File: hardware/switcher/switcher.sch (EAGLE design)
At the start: 3 parts, among them IC1 L293E

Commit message: update schematics
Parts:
- removed G1: AB9V, battery:AB9V
- added BAT1: (no value), SparkFun-Connectors:BC9VPC
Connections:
- net P1.3 renamed P2.4
- net 9V: now also BAT1.V+; no longer G1.+
- net GND: now also BAT1.V-; no longer G1.-
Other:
- note added: "5V Regulator"
- note added: "9V Battery Holder"
- note added: "Board for holding motor driver and power source and connects both to the motor and to the Green Board"
- note added: "Derailleurs Switcher Board Alice Stevens and Mackenzie Binns"
- note added: "H-Bridge Motor Controller"
- note added: "LM7805"
- note added: "This board connects to the Green Board via mated headers."
- note removed: "Custom board for motor module - Alice Stevens"

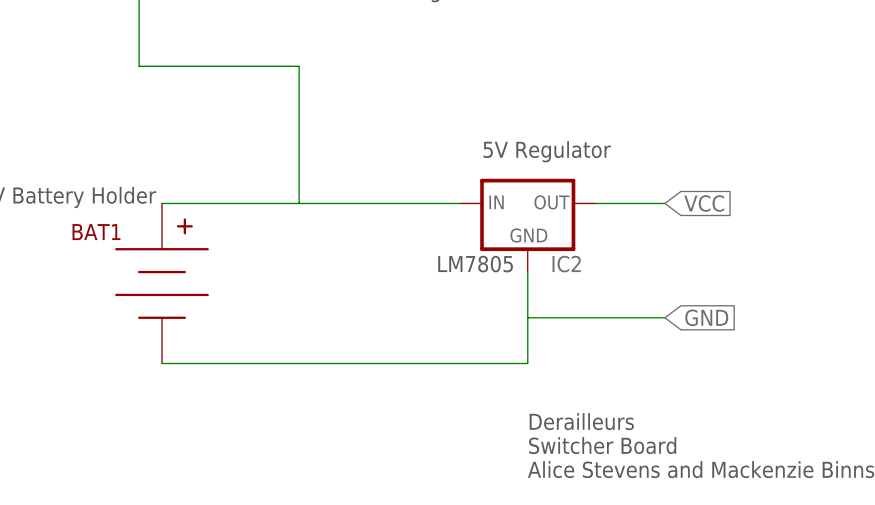
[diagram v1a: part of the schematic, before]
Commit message: add capacitors
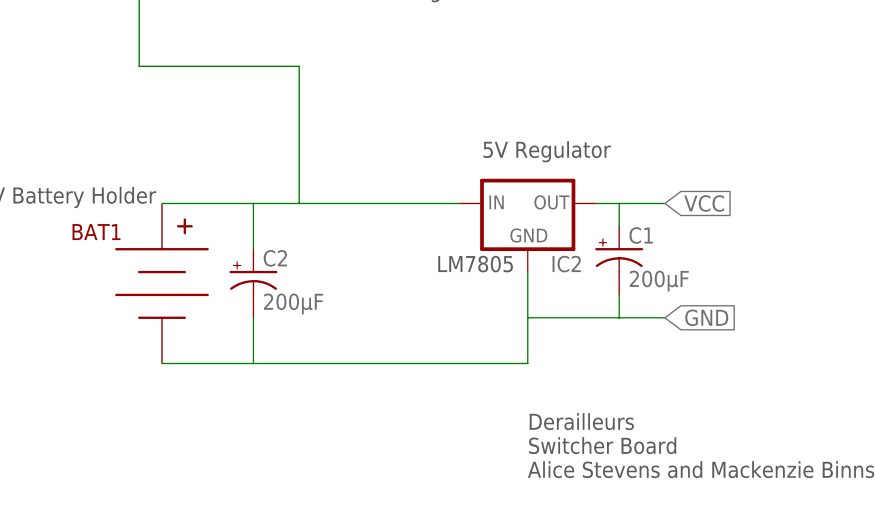
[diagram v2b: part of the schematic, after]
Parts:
- added C1, C2: 200µF, SparkFun-Capacitors:CAP_POLPTH1
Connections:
- net 9V: now also C2.+
- net GND: now also C1.-, C2.-
- net VCC: now also C1.+
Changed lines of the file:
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@@
 <part name="IC2" library="v-reg" deviceset="78XXL" device=""/>
 <part name="BAT1" library="SparkFun-Connectors" deviceset="BC9VPC" device=""/>
+<part name="C1" library="SparkFun-Capacitors" deviceset="CAP_POL" device="PTH1" value="200µF"/>
+<part name="C2" library="SparkFun-Capacitors" deviceset="CAP_POL" device="PTH1" value="200µF"/>
 </parts>
 <sheets>
@@
 <instance part="IC2" gate="A" x="76.2" y="10.16"/>
 <instance part="BAT1" gate="G$1" x="35.56" y="2.54"/>
+<instance part="C1" gate="G$1" x="86.36" y="5.08"/>
+<instance part="C2" gate="G$1" x="45.72" y="2.54"/>
 </instances>
 <busses>
@@
 <segment>
 <pinref part="IC2" gate="A" pin="OUT"/>
-<wire x1="83.82" y1="10.16" x2="91.44" y2="10.16" width="0.1524" layer="91"/>
+<wire x1="83.82" y1="10.16" x2="86.36" y2="10.16" width="0.1524" layer="91"/>
 <label x="91.44" y="10.16" size="1.778" layer="95" xref="yes"/>
+<pinref part="C1" gate="G$1" pin="+"/>
+<wire x1="86.36" y1="10.16" x2="91.44" y2="10.16" width="0.1524" layer="91"/>
+<wire x1="86.36" y1="7.62" x2="86.36" y2="10.16" width="0.1524" layer="91"/>
 </segment>
 </net>
@@
 <pinref part="IC2" gate="A" pin="GND"/>
 <wire x1="76.2" y1="-2.54" x2="76.2" y2="2.54" width="0.1524" layer="91"/>
-<wire x1="76.2" y1="-2.54" x2="91.44" y2="-2.54" width="0.1524" layer="91"/>
+<wire x1="76.2" y1="-2.54" x2="86.36" y2="-2.54" width="0.1524" layer="91"/>
 <label x="91.44" y="-2.54" size="1.778" layer="95" xref="yes"/>
 <pinref part="BAT1" gate="G$1" pin="V-"/>
-<wire x1="35.56" y1="-7.62" x2="76.2" y2="-7.62" width="0.1524" layer="91"/>
+<wire x1="86.36" y1="-2.54" x2="91.44" y2="-2.54" width="0.1524" layer="91"/>
+<wire x1="35.56" y1="-7.62" x2="45.72" y2="-7.62" width="0.1524" layer="91"/>
+<wire x1="45.72" y1="-7.62" x2="76.2" y2="-7.62" width="0.1524" layer="91"/>
 <wire x1="76.2" y1="-7.62" x2="76.2" y2="-2.54" width="0.1524" layer="91"/>
+<pinref part="C2" gate="G$1" pin="-"/>
+<wire x1="45.72" y1="-2.54" x2="45.72" y2="-7.62" width="0.1524" layer="91"/>
+<pinref part="C1" gate="G$1" pin="-"/>
+<wire x1="86.36" y1="0" x2="86.36" y2="-2.54" width="0.1524" layer="91"/>
 </segment>
 </net>
@@
 <wire x1="33.02" y1="25.4" x2="50.8" y2="25.4" width="0.1524" layer="91"/>
 <pinref part="IC2" gate="A" pin="IN"/>
-<wire x1="35.56" y1="10.16" x2="50.8" y2="10.16" width="0.1524" layer="91"/>
+<wire x1="35.56" y1="10.16" x2="45.72" y2="10.16" width="0.1524" layer="91"/>
+<wire x1="45.72" y1="10.16" x2="50.8" y2="10.16" width="0.1524" layer="91"/>
 <wire x1="50.8" y1="10.16" x2="68.58" y2="10.16" width="0.1524" layer="91"/>
 <wire x1="50.8" y1="25.4" x2="50.8" y2="10.16" width="0.1524" layer="91"/>
 <pinref part="BAT1" gate="G$1" pin="V+"/>
+<pinref part="C2" gate="G$1" pin="+"/>
+<wire x1="45.72" y1="5.08" x2="45.72" y2="10.16" width="0.1524" layer="91"/>
 </segment>
 </net>

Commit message: finish boards
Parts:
- removed BAT1: (no value), SparkFun-Connectors:BC9VPC
- added BLUE, RED, WHITE, YELLOW: (no value), SparkFun-Connectors:M01PTH
- added GND, VCC: (no value), SparkFun-Connectors:M03PTH
- added J1, J2: (no value), SparkFun-Connectors:M20
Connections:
- removed net P2.4: IC1.4A
- new net P2.5: IC1.4A, J1.3
- net 9V: no longer BAT1.V+
- net GND: now also GND.1, GND.2, GND.3; no longer BAT1.V-
- net MOTOR-BLUE: now also BLUE.1
- net MOTOR-RED: now also RED.1
- net MOTOR-WHITE: now also WHITE.1
- net MOTOR-YELLOW: now also YELLOW.1
- net P3.4: now also J1.10
- net P3.5: now also J1.11
- net P3.6: now also J1.12
- net VCC: now also VCC.1, VCC.2, VCC.3
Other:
- note removed: "9V Battery Holder"
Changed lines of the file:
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@@
 <part name="IC1" library="texas" deviceset="L293E" device=""/>
 <part name="IC2" library="v-reg" deviceset="78XXL" device=""/>
-<part name="BAT1" library="SparkFun-Connectors" deviceset="BC9VPC" device=""/>
 <part name="C1" library="SparkFun-Capacitors" deviceset="CAP_POL" device="PTH1" value="200µF"/>
 <part name="C2" library="SparkFun-Capacitors" deviceset="CAP_POL" device="PTH1" value="200µF"/>
+<part name="J1" library="SparkFun-Connectors" deviceset="M20" device=""/>
+<part name="J2" library="SparkFun-Connectors" deviceset="M20" device=""/>
+<part name="GND" library="SparkFun-Connectors" deviceset="M03" device="PTH"/>
+<part name="VCC" library="SparkFun-Connectors" deviceset="M03" device="PTH"/>
+<part name="RED" library="SparkFun-Connectors" deviceset="M01" device="PTH"/>
+<part name="YELLOW" library="SparkFun-Connectors" deviceset="M01" device="PTH"/>
+<part name="BLUE" library="SparkFun-Connectors" deviceset="M01" device="PTH"/>
+<part name="WHITE" library="SparkFun-Connectors" deviceset="M01" device="PTH"/>
 </parts>
 <sheets>
 <sheet>
 <plain>
-<frame x1="-7.62" y1="-25.4" x2="119.38" y2="96.52" columns="8" rows="5" layer="91"/>
 <text x="-2.54" y="88.9" size="1.778" layer="97">Board for holding motor driver and power source and connects both to the motor and to the Green Board</text>
 <text x="58.42" y="33.02" size="1.778" layer="97">H-Bridge Motor Controller</text>
 <text x="66.04" y="2.54" size="1.778" layer="97">LM7805</text>
 <text x="71.12" y="15.24" size="1.778" layer="97">5V Regulator</text>
-<text x="15.24" y="10.16" size="1.778" layer="97">9V Battery Holder</text>
 <text x="-2.54" y="83.82" size="1.778" layer="97">This board connects to the Green Board via mated headers.</text>
-<text x="76.2" y="-20.32" size="1.778" layer="97">Derailleurs
+<text x="129.54" y="-20.32" size="1.778" layer="97">Derailleurs
 Switcher Board
 Alice Stevens and Mackenzie Binns</text>
+<frame x1="-20.32" y1="-27.94" x2="180.34" y2="96.52" columns="8" rows="5" layer="91"/>
 </plain>
 <instances>
 <instance part="IC1" gate="G$1" x="55.88" y="55.88"/>
 <instance part="IC2" gate="A" x="76.2" y="10.16"/>
-<instance part="BAT1" gate="G$1" x="35.56" y="2.54"/>
 <instance part="C1" gate="G$1" x="86.36" y="5.08"/>
 <instance part="C2" gate="G$1" x="45.72" y="2.54"/>
+<instance part="J1" gate="G$1" x="114.3" y="22.86"/>
+<instance part="J2" gate="G$1" x="147.32" y="22.86"/>
+<instance part="GND" gate="J$1" x="116.84" y="7.62"/>
+<instance part="VCC" gate="J$1" x="149.86" y="7.62"/>
+<instance part="RED" gate="G$1" x="-10.16" y="7.62"/>
+<instance part="YELLOW" gate="G$1" x="-10.16" y="0"/>
+<instance part="BLUE" gate="G$1" x="-10.16" y="15.24"/>
+<instance part="WHITE" gate="G$1" x="-10.16" y="22.86"/>
 </instances>
 <busses>
@@
 <wire x1="86.36" y1="7.62" x2="86.36" y2="10.16" width="0.1524" layer="91"/>
 </segment>
+<segment>
+<pinref part="VCC" gate="J$1" pin="1"/>
+<wire x1="157.48" y1="5.08" x2="160.02" y2="5.08" width="0.1524" layer="91"/>
+<wire x1="160.02" y1="5.08" x2="160.02" y2="7.62" width="0.1524" layer="91"/>
+<pinref part="VCC" gate="J$1" pin="2"/>
+<wire x1="157.48" y1="7.62" x2="160.02" y2="7.62" width="0.1524" layer="91"/>
+<pinref part="VCC" gate="J$1" pin="3"/>
+<wire x1="157.48" y1="10.16" x2="160.02" y2="10.16" width="0.1524" layer="91"/>
+<wire x1="160.02" y1="10.16" x2="160.02" y2="7.62" width="0.1524" layer="91"/>
+<label x="160.02" y="7.62" size="1.778" layer="95" xref="yes"/>
+</segment>
 </net>
 <net name="P3.4" class="0">
@@
 <label x="33.02" y="68.58" size="1.778" layer="95" rot="MR0" xref="yes"/>
 </segment>
+<segment>
+<pinref part="J1" gate="G$1" pin="10"/>
+<wire x1="124.46" y1="50.8" x2="127" y2="50.8" width="0.1524" layer="91"/>
+<label x="127" y="50.8" size="1.778" layer="95" xref="yes"/>
+</segment>
 </net>
 <net name="MOTOR-RED" class="0">
@@
 <wire x1="40.64" y1="63.5" x2="33.02" y2="63.5" width="0.1524" layer="91"/>
 <label x="33.02" y="63.5" size="1.778" layer="95" rot="MR0" xref="yes"/>
+</segment>
+<segment>
+<pinref part="RED" gate="G$1" pin="1"/>
+<wire x1="-2.54" y1="7.62" x2="2.54" y2="7.62" width="0.1524" layer="91"/>
+<label x="2.54" y="7.62" size="1.778" layer="95" xref="yes"/>
 </segment>
 </net>
@@
 <wire x1="76.2" y1="-2.54" x2="86.36" y2="-2.54" width="0.1524" layer="91"/>
 <label x="91.44" y="-2.54" size="1.778" layer="95" xref="yes"/>
-<pinref part="BAT1" gate="G$1" pin="V-"/>
 <wire x1="86.36" y1="-2.54" x2="91.44" y2="-2.54" width="0.1524" layer="91"/>
 <wire x1="35.56" y1="-7.62" x2="45.72" y2="-7.62" width="0.1524" layer="91"/>
@@
 <pinref part="C1" gate="G$1" pin="-"/>
 <wire x1="86.36" y1="0" x2="86.36" y2="-2.54" width="0.1524" layer="91"/>
+<label x="35.56" y="-7.62" size="1.778" layer="95" rot="R180" xref="yes"/>
+</segment>
+<segment>
+<pinref part="GND" gate="J$1" pin="1"/>
+<wire x1="124.46" y1="5.08" x2="127" y2="5.08" width="0.1524" layer="91"/>
+<wire x1="127" y1="5.08" x2="127" y2="7.62" width="0.1524" layer="91"/>
+<pinref part="GND" gate="J$1" pin="2"/>
+<wire x1="127" y1="7.62" x2="124.46" y2="7.62" width="0.1524" layer="91"/>
+<pinref part="GND" gate="J$1" pin="3"/>
+<wire x1="124.46" y1="10.16" x2="127" y2="10.16" width="0.1524" layer="91"/>
+<wire x1="127" y1="10.16" x2="127" y2="7.62" width="0.1524" layer="91"/>
+<label x="127" y="7.62" size="1.778" layer="95" xref="yes"/>
 </segment>
 </net>
@@
 <label x="33.02" y="48.26" size="1.778" layer="95" rot="MR0" xref="yes"/>
 </segment>
+<segment>
+<pinref part="BLUE" gate="G$1" pin="1"/>
+<wire x1="-2.54" y1="15.24" x2="2.54" y2="15.24" width="0.1524" layer="91"/>
+<label x="2.54" y="15.24" size="1.778" layer="95" xref="yes"/>
+</segment>
 </net>
 <net name="P3.5" class="0">
@@
 <wire x1="40.64" y1="43.18" x2="33.02" y2="43.18" width="0.1524" layer="91"/>
 <label x="33.02" y="43.18" size="1.778" layer="95" rot="MR0" xref="yes"/>
+</segment>
+<segment>
+<pinref part="J1" gate="G$1" pin="11"/>
+<wire x1="124.46" y1="53.34" x2="134.62" y2="53.34" width="0.1524" layer="91"/>
+<label x="134.62" y="53.34" size="1.778" layer="95" xref="yes"/>
 </segment>
 </net>
@@
 <wire x1="50.8" y1="10.16" x2="68.58" y2="10.16" width="0.1524" layer="91"/>
 <wire x1="50.8" y1="25.4" x2="50.8" y2="10.16" width="0.1524" layer="91"/>
-<pinref part="BAT1" gate="G$1" pin="V+"/>
 <pinref part="C2" gate="G$1" pin="+"/>
 <wire x1="45.72" y1="5.08" x2="45.72" y2="10.16" width="0.1524" layer="91"/>
-</segment>
-</net>
-<net name="P2.4" class="0">
+<label x="35.56" y="10.16" size="1.778" layer="95" rot="R180" xref="yes"/>
+</segment>
+</net>
+<net name="P2.5" class="0">
 <segment>
 <pinref part="IC1" gate="G$1" pin="4A"/>
@@
 <label x="78.74" y="68.58" size="1.778" layer="95" xref="yes"/>
 </segment>
+<segment>
+<pinref part="J1" gate="G$1" pin="3"/>
+<wire x1="124.46" y1="33.02" x2="127" y2="33.02" width="0.1524" layer="91"/>
+<label x="127" y="33.02" size="1.778" layer="95" xref="yes"/>
+</segment>
 </net>
 <net name="MOTOR-YELLOW" class="0">
@@
 <label x="78.74" y="63.5" size="1.778" layer="95" xref="yes"/>
 </segment>
+<segment>
+<pinref part="YELLOW" gate="G$1" pin="1"/>
+<wire x1="-2.54" y1="0" x2="2.54" y2="0" width="0.1524" layer="91"/>
+<label x="2.54" y="0" size="1.778" layer="95" xref="yes"/>
+</segment>
 </net>
 <net name="MOTOR-WHITE" class="0">
@@
 <label x="78.74" y="48.26" size="1.778" layer="95" xref="yes"/>
 </segment>
+<segment>
+<pinref part="WHITE" gate="G$1" pin="1"/>
+<wire x1="-2.54" y1="22.86" x2="2.54" y2="22.86" width="0.1524" layer="91"/>
+<label x="2.54" y="22.86" size="1.778" layer="95" xref="yes"/>
+</segment>
 </net>
 <net name="P3.6" class="0">
@@
 <label x="78.74" y="43.18" size="1.778" layer="95" xref="yes"/>
 </segment>
-</net>
+<segment>
+<pinref part="J1" gate="G$1" pin="12"/>
+<wire x1="124.46" y1="55.88" x2="127" y2="55.88" width="0.1524" layer="91"/>
+<label x="127" y="55.88" size="1.778" layer="95" xref="yes"/>
+</segment>
+</net>

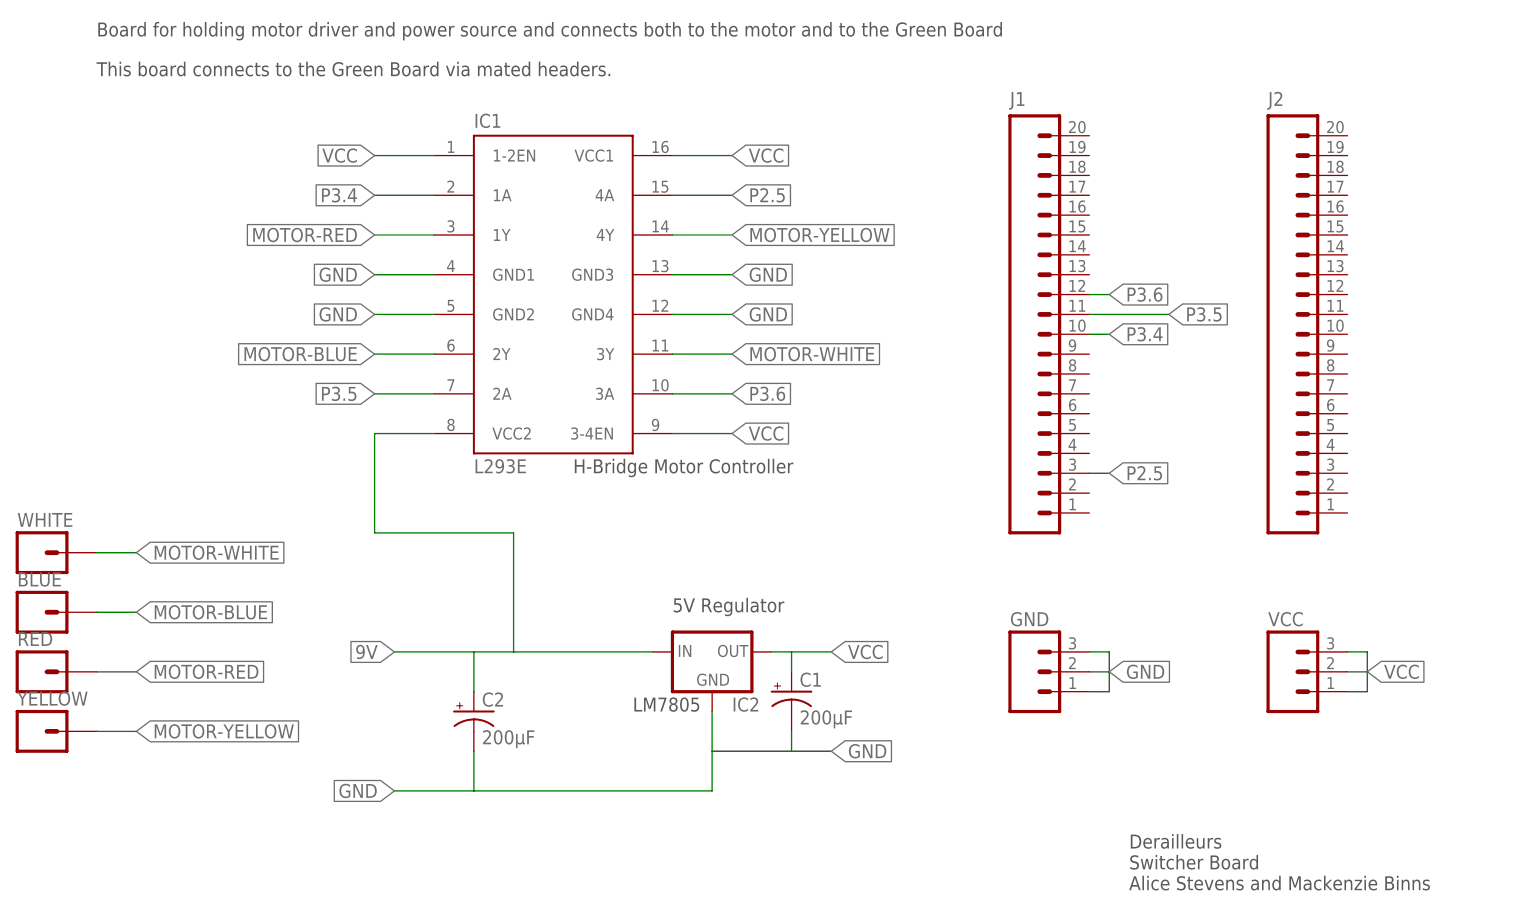
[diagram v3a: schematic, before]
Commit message: Finish routing all boards, schematics are consitant, and all deliverable requirements are met..
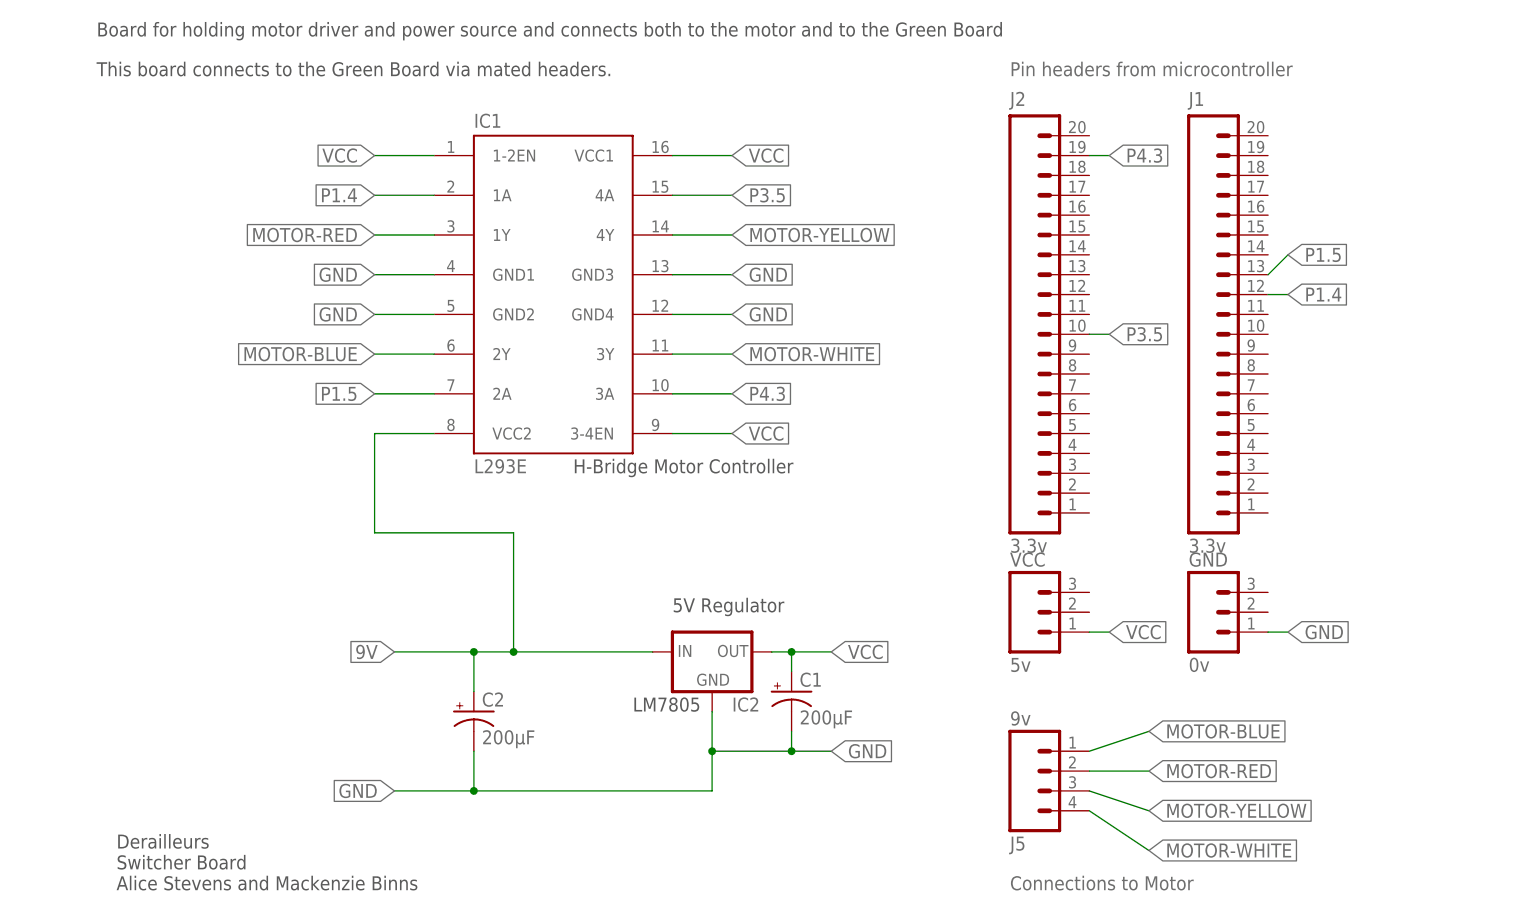
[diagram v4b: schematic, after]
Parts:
- removed BLUE, RED, WHITE, YELLOW: (no value), SparkFun-Connectors:M01PTH
- added J5: 9v, SparkFun-Connectors:M04PTH
- GND: value (none) -> 0v
- J1, J2: value (none) -> 3.3v
- VCC: value (none) -> 5v
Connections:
- removed net P2.5: IC1.4A, J1.3
- removed net P3.4: IC1.1A, J1.10
- removed net P3.6: IC1.3A, J1.12
- new net P1.4: IC1.1A, J1.12
- new net P1.5: IC1.2A, J1.13
- new net P4.3: IC1.3A, J2.19
- net GND: no longer GND.2, GND.3
- net MOTOR-BLUE: now also J5.1; no longer BLUE.1
- net MOTOR-RED: now also J5.2; no longer RED.1
- net MOTOR-WHITE: now also J5.4; no longer WHITE.1
- net MOTOR-YELLOW: now also J5.3; no longer YELLOW.1
- net P3.5: now also IC1.4A, J2.10; no longer IC1.2A, J1.11
- net VCC: no longer VCC.2, VCC.3
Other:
- note added: "Connections to Motor"
- note added: "Pin headers from microcontroller"
- moved on the sheet: GND, J1, J2, VCC
